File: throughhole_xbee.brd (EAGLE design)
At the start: 204.4 x 88.6 mm, 134 parts, among them IC1 P82B715D, J1 6473427-1, J2 VR10S05, Q1 MOSFET-NCHANNELSMD, Q2 MOSFET-NCHANNELSMD, SW1 CTS_ELECTROCOMPONENTS_204-211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, SW2 CTS_ELECTROCOMPONENTS_204-211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, U1 XC6220B331MR-G, U4 ARDUINO_R3_SHIELD, U6 ADS1119IPWT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

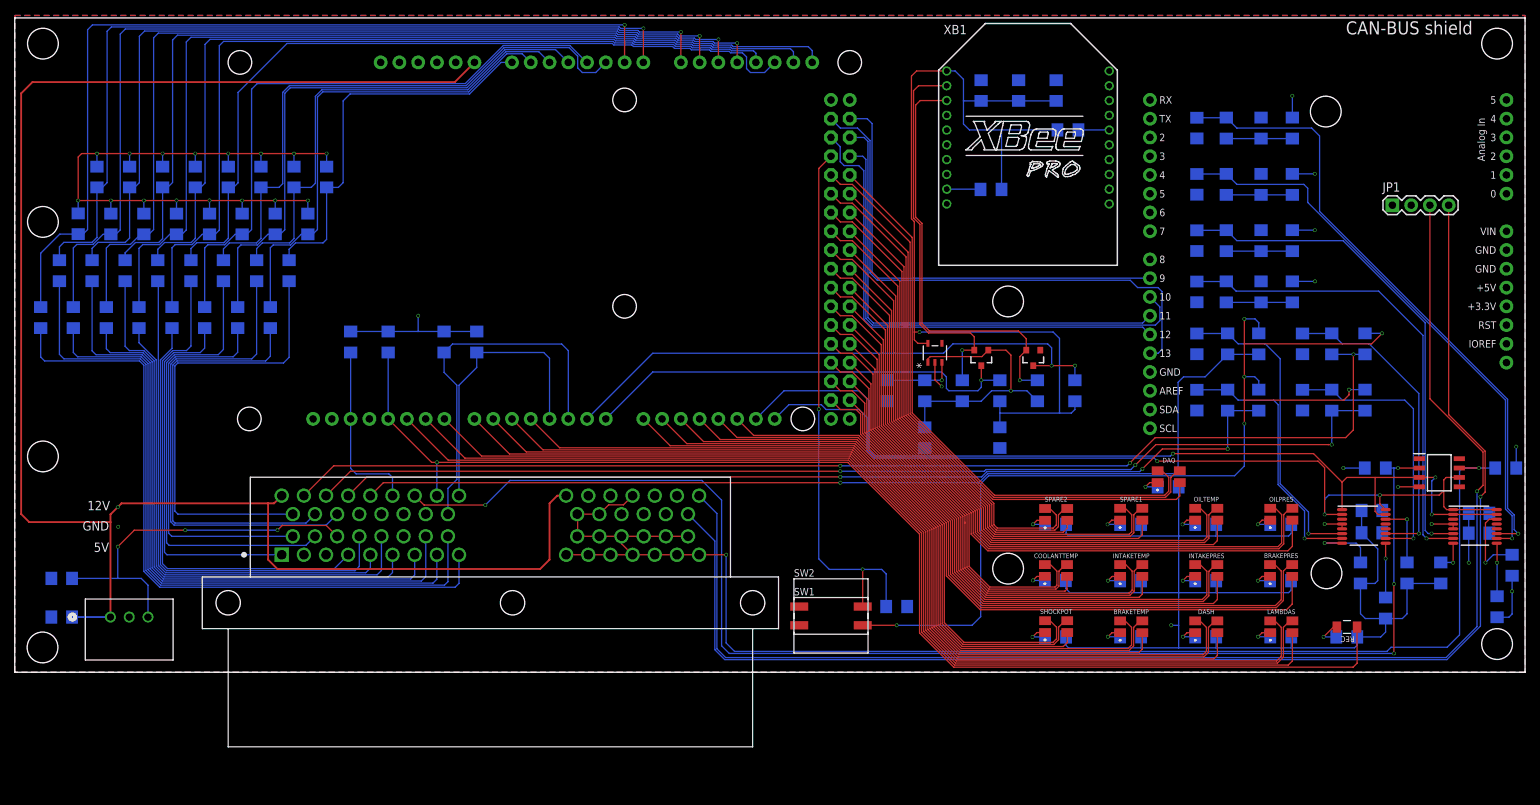
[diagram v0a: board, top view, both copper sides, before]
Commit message: Moved the connector to be flush & pushed to Fusion 360
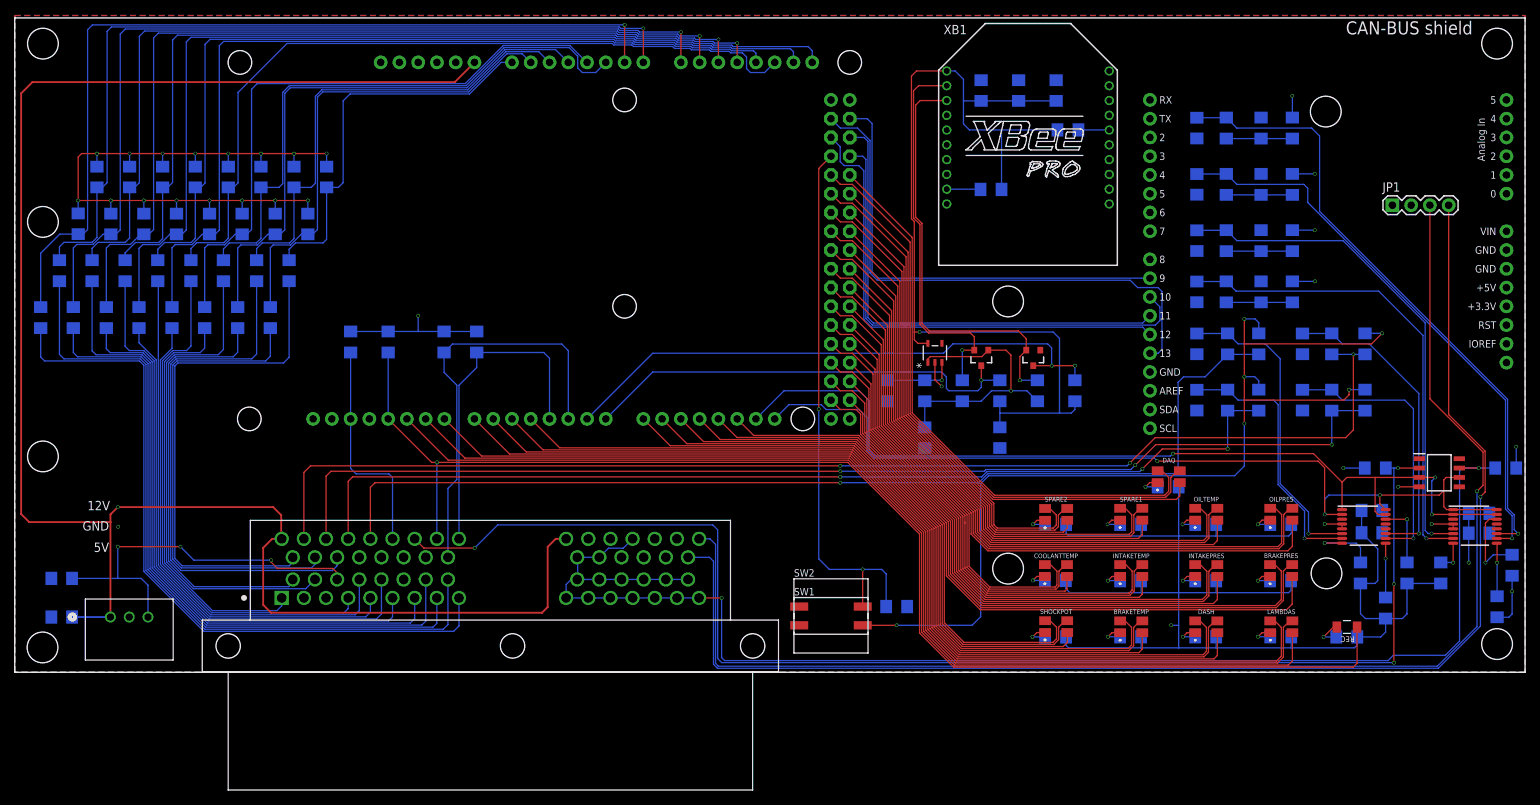
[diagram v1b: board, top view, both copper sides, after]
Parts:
- moved J1 5.84 mm to (53.4, 56.9)
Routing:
- net SG_41: track 160.5 -> 168.2 mm
- net A0IN: track 62.0 -> 69.6 mm
- net SG_31: track 148.1 -> 155.5 mm
- net 12V: track 233.0 -> 240.0 mm
- net SG_21: track 131.1 -> 138.0 mm
- net SG_11: track 135.1 -> 141.6 mm
- net A2IN: track 66.7 -> 73.1 mm
- net A1IN: track 58.5 -> 64.7 mm
- net FR_WS: track 38.8 -> 44.6 mm
- net CALIB: track 24.3 -> 30.2 mm
- net FL_WS: track 50.0 -> 55.8 mm
- net REC: track 171.5 -> 177.4 mm
- net A3IN: track 53.2 -> 58.9 mm
- net A4IN: track 50.7 -> 56.0 mm
- net A5IN: track 62.8 -> 66.8 mm
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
